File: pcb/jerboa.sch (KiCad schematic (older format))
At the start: 25 parts, among them P101 SWD_TC, U101 STM32L051K8U6

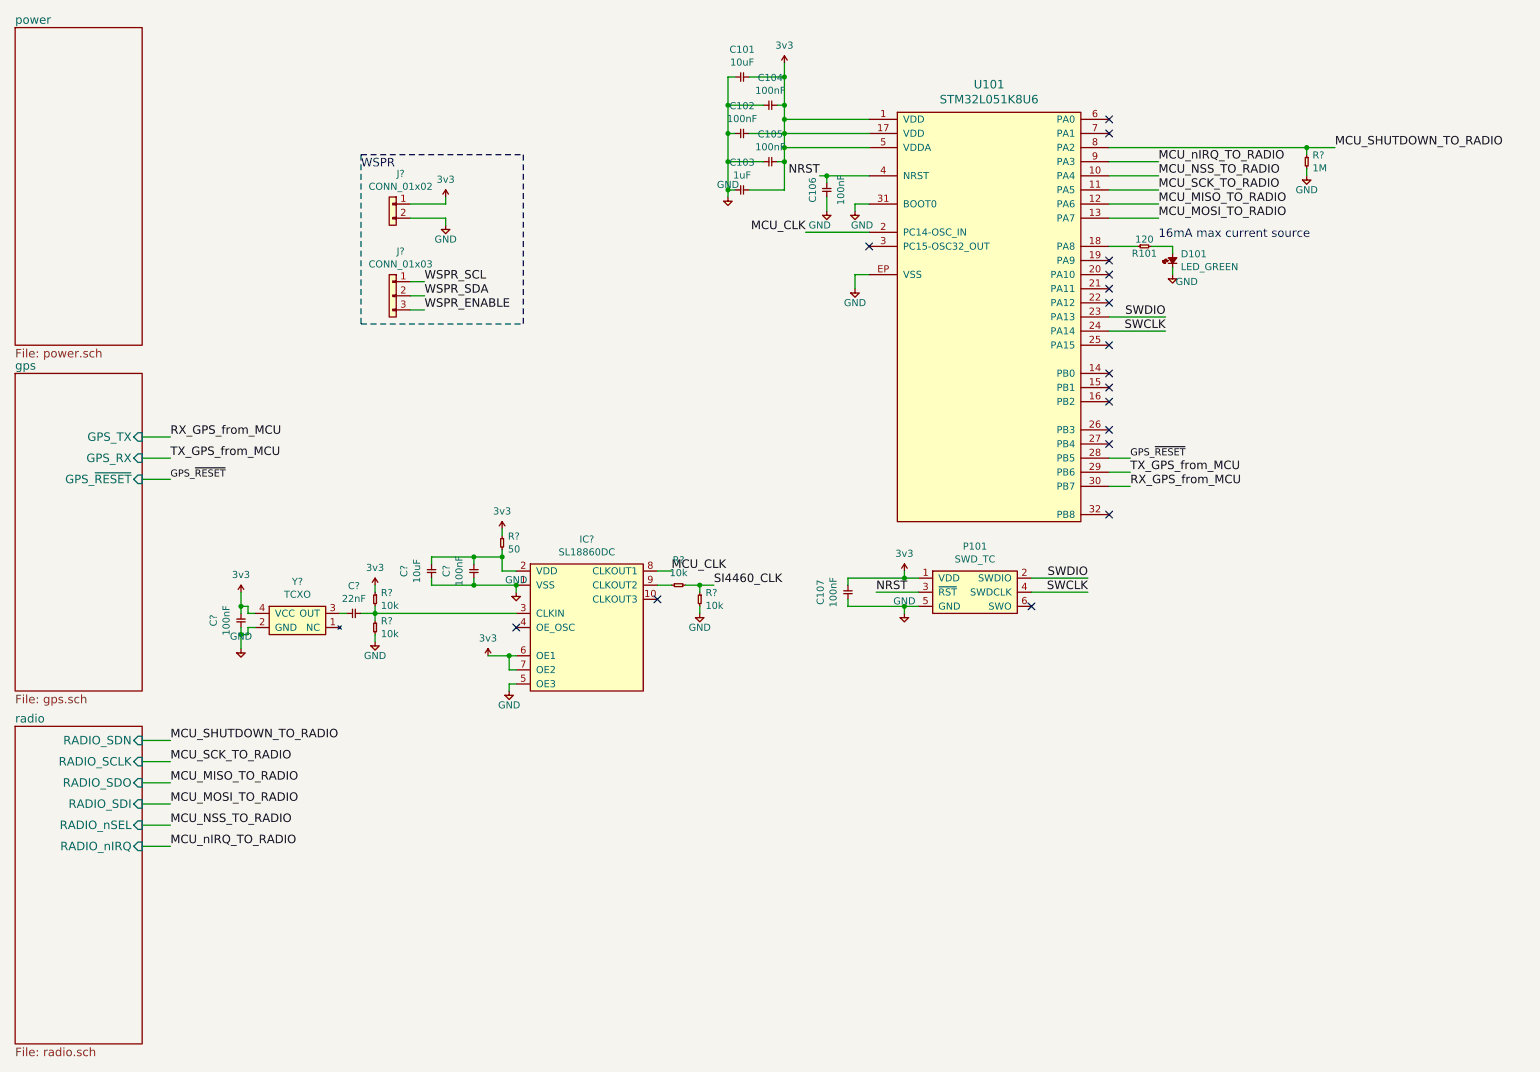
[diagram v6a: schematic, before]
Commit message: WIP: create and add componenents for the micrf rtty radio, also do some work on schematic
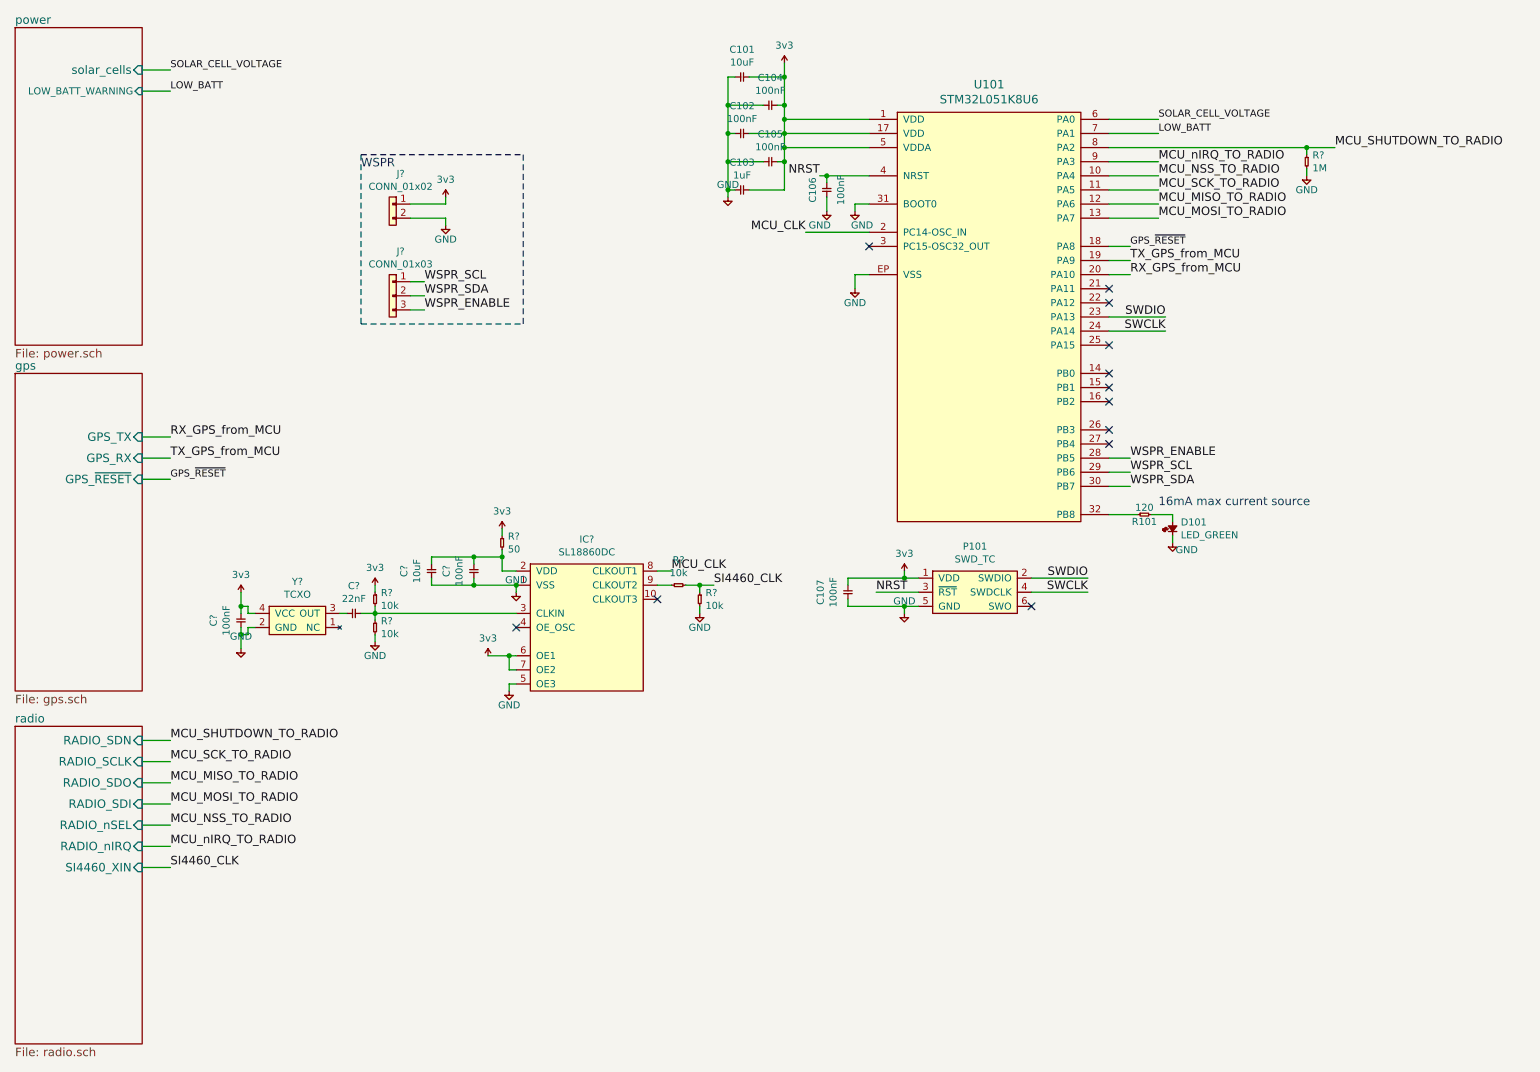
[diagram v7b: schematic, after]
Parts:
- J?: Farnell (none) -> 1593459
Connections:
- net GPS_~RESET: now also U101.18 (PA8); no longer U101.28 (PB5)
- net RX_GPS_from_MCU: now also U101.20 (PA10); no longer U101.30 (PB7)
- net TX_GPS_from_MCU: now also U101.19 (PA9); no longer U101.29 (PB6)
- net WSPR_ENABLE: now also U101.28 (PB5)
- net WSPR_SCL: now also U101.29 (PB6)
- net WSPR_SDA: now also U101.30 (PB7)
- net at R101.1: now also U101.32 (PB8); no longer U101.18 (PA8)
- net SOLAR_CELL_VOLTAGE: now reaches U101.6 (PA0)
- net LOW_BATT: now reaches U101.7 (PA1)
- no-connect marks 17 -> 12
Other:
- moved on the sheet: D101, R101
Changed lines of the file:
@@
 F0 "power" 60
 F1 "power.sch" 60
+F2 "solar_cells" I R 1400 800 60
+F3 "LOW_BATT_WARNING" I R 1400 950 50
 $EndSheet
 $Sheet
@@
 $EndSheet
 $Comp
-L STM32L051K8U6:STM32L051K8U6 U101
-U 1 1 5A37D9A9
-P 7400 2500
-F 0 "U101" H 7400 4097 60  0000 C CNN
-F 1 "STM32L051K8U6" H 7400 3991 60  0000 C CNN
-F 2 "agg:QFN-32-EP-ST" H 7050 800 60  0001 L CNN
-F 3 "http://www.st.com/resource/en/datasheet/stm32l051t8.pdf" H 7050 700 60  0001 L CNN
-F 4 "2488323" H 7050 600 60  0001 L CNN "Farnell"
-	1    7400 2500
-	1    0    0    -1
-$EndComp
-$Comp
 L agg-kicad:GND #PWR01
 U 1 1 5A3E3DF5
@@
 L agg-kicad:LED D101
 U 1 1 5A3E82EC
-P 8700 2200
-F 0 "D101" V 8796 2142 50  0000 R CNN
-F 1 "LED_GREEN" V 8705 2142 50  0000 R CNN
-F 2 "agg:0603-LED" H 8700 2200 50  0001 C CNN
-F 3 "http://www.farnell.com/datasheets/2057314.pdf?_ga=2.205110360.971487712.1514028244-506493331.1509210212&_gac=1.118829563.1511728794.Cj0KCQiA6enQBRDUARIsAGs1YQiJE2FAEjDkPfQxMJDRdXOREIvhi5-XX62hZWxB6j9IyKlXVrhl04oaArmMEALw_wcB" H 8700 2200 50  0001 C CNN
-F 4 "2575345" H 8700 2200 60  0001 C CNN "Farnell"
-	1    8700 2200
+P 8700 4100
+F 0 "D101" V 8796 4042 50  0000 R CNN
+F 1 "LED_GREEN" V 8705 4042 50  0000 R CNN
+F 2 "agg:0603-LED" H 8700 4100 50  0001 C CNN
+F 3 "http://www.farnell.com/datasheets/2057314.pdf?_ga=2.205110360.971487712.1514028244-506493331.1509210212&_gac=1.118829563.1511728794.Cj0KCQiA6enQBRDUARIsAGs1YQiJE2FAEjDkPfQxMJDRdXOREIvhi5-XX62hZWxB6j9IyKlXVrhl04oaArmMEALw_wcB" H 8700 4100 50  0001 C CNN
+F 4 "2575345" H 8700 4100 60  0001 C CNN "Farnell"
+	1    8700 4100
 	0    -1   -1   0
 $EndComp
@@
 L agg-kicad:R R101
 U 1 1 5A3E86C8
-P 8450 2050
-F 0 "R101" H 8500 2000 50  0000 C CNN
-F 1 "120" H 8500 2100 50  0000 C CNN
-F 2 "agg:0402" H 8450 2050 50  0001 C CNN
-F 3 "" H 8450 2050 50  0001 C CNN
-F 4 "9239120" H 8450 2050 60  0001 C CNN "Farnell"
-	1    8450 2050
+P 8450 3950
+F 0 "R101" H 8500 3900 50  0000 C CNN
+F 1 "120" H 8500 4000 50  0000 C CNN
+F 2 "agg:0402" H 8450 3950 50  0001 C CNN
+F 3 "" H 8450 3950 50  0001 C CNN
+F 4 "9239120" H 8450 3950 60  0001 C CNN "Farnell"
+	1    8450 3950
 	1    0    0    -1
 $EndComp
@@
 L agg-kicad:GND #PWR08
 U 1 1 5A3EA11D
-P 8700 2250
-F 0 "#PWR08" H 8570 2290 50  0001 L CNN
-F 1 "GND" H 8800 2200 50  0000 C CNN
-F 2 "" H 8700 2250 60  0001 C CNN
-F 3 "" H 8700 2250 60  0001 C CNN
-	1    8700 2250
-	1    0    0    -1
-$EndComp
-Text Notes 8600 2000 0    60   ~ 0
+P 8700 4150
+F 0 "#PWR08" H 8570 4190 50  0001 L CNN
+F 1 "GND" H 8800 4100 50  0000 C CNN
+F 2 "" H 8700 4150 60  0001 C CNN
+F 3 "" H 8700 4150 60  0001 C CNN
+	1    8700 4150
+	1    0    0    -1
+$EndComp
+Text Notes 8600 3900 0    60   ~ 0
 16mA max current source
 $Comp
@@
 Connection ~ 6250 1550
 Wire Wire Line
-	8250 2050 8450 2050
-Wire Wire Line
-	8700 2250 8700 2200
-Wire Wire Line
-	8700 2100 8700 2050
-Wire Wire Line
-	8700 2050 8550 2050
+	8250 3950 8450 3950
+Wire Wire Line
+	8700 4150 8700 4100
+Wire Wire Line
+	8700 4000 8700 3950
+Wire Wire Line
+	8700 3950 8550 3950
 Wire Wire Line
 	6450 1750 6550 1750
@@
 Wire Wire Line
 	6200 1550 6250 1550
-Text Label 8400 3650 0    60   ~ 0
+Text Label 8400 2150 0    60   ~ 0
 TX_GPS_from_MCU
-Text Label 8400 3750 0    60   ~ 0
+Text Label 8400 2250 0    60   ~ 0
 RX_GPS_from_MCU
-Wire Wire Line
-	8250 3750 8400 3750
 NoConn ~ 6550 2050
-NoConn ~ 8250 1150
-NoConn ~ 8250 1250
-NoConn ~ 8250 2150
-NoConn ~ 8250 2250
 NoConn ~ 8250 2350
 NoConn ~ 8250 2450
@@
 NoConn ~ 8250 3150
 NoConn ~ 8250 3350
-NoConn ~ 8250 3950
 Wire Wire Line
 	6400 4600 6800 4600
@@
 F6 "RADIO_nSEL" I R 1400 6150 60
 F7 "RADIO_nIRQ" I R 1400 6300 60
+F8 "SI4460_XIN" I R 1400 6450 60
 $EndSheet
 Wire Wire Line
@@
 Text Label 1600 6300 0    60   ~ 0
 MCU_nIRQ_TO_RADIO
-Wire Wire Line
-	8400 3650 8250 3650
 $Comp
 L agg-kicad:R R?
@@
 Text Label 1600 3700 0    50   ~ 0
 GPS_~RESET
-Text Label 8400 3550 0    50   ~ 0
+Text Label 8400 2050 0    50   ~ 0
 GPS_~RESET
 Wire Wire Line
-	8400 3550 8250 3550
+	8400 2050 8250 2050
 $Comp
 L agg-kicad:SL18860DC IC?
@@
 F 2 "" H 3200 2300 50  0001 C CNN
 F 3 "" H 3200 2300 50  0001 C CNN
+F 4 "1593459" H 3200 2300 50  0001 C CNN "Farnell"
 	1    3200 2300
 	1    0    0    -1
@@
 Wire Wire Line
 	2850 4650 2800 4650
+Text Label 8400 3650 0    60   ~ 0
+WSPR_SCL
+Text Label 8400 3750 0    60   ~ 0
+WSPR_SDA
+Text Label 8400 3550 0    60   ~ 0
+WSPR_ENABLE
+Wire Wire Line
+	8250 2150 8400 2150
+Wire Wire Line
+	8400 2250 8250 2250
+$Comp
+L STM32L051K8U6:STM32L051K8U6 U101
+U 1 1 5A37D9A9
+P 7400 2500
+F 0 "U101" H 7400 4097 60  0000 C CNN
+F 1 "STM32L051K8U6" H 7400 3991 60  0000 C CNN
+F 2 "agg:QFN-32-EP-ST" H 7050 800 60  0001 L CNN
+F 3 "http://www.st.com/resource/en/datasheet/stm32l051t8.pdf" H 7050 700 60  0001 L CNN
+F 4 "2488323" H 7050 600 60  0001 L CNN "Farnell"
+	1    7400 2500
+	1    0    0    -1
+$EndComp
+Wire Wire Line
+	8250 3550 8400 3550
+Wire Wire Line
+	8400 3650 8250 3650
+Wire Wire Line
+	8250 3750 8400 3750
+Wire Wire Line
+	1400 950  1600 950
+Wire Wire Line
+	1600 800  1400 800
+Text Label 8600 1150 0    50   ~ 0
+SOLAR_CELL_VOLTAGE
+Wire Wire Line
+	8600 1150 8250 1150
+Text Label 8600 1250 0    50   ~ 0
+LOW_BATT
+Wire Wire Line
+	8250 1250 8600 1250
+Text Label 1600 800  0    50   ~ 0
+SOLAR_CELL_VOLTAGE
+Text Label 1600 950  0    50   ~ 0
+LOW_BATT
+Text Label 1600 6450 0    60   ~ 0
+SI4460_CLK
+Wire Wire Line
+	1600 6450 1400 6450
 $EndSCHEMATC

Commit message: Finish schematic, generate first BOM
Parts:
- added R7, R8: 4k7, agg:0402, symbol agg-kicad:R
- C1, C4: renamed from C?; Farnell 1288282 -> 2533923
- C10: renamed from C106; Farnell 1288282 -> 2533923
- C11: renamed from C107; Farnell 1288282 -> 2533923
- C2: renamed from C?; Farnell 1288282 -> 1828865
- C3: renamed from C?; Farnell 1288282 -> 2611904
- C5: renamed from C101; footprint (none) -> agg:0402; Farnell Value -> 2611904
- C6: renamed from C102; Farnell 1288282 -> 2533923
- C7: renamed from C103; Farnell 1327658 -> 1758879
- C8: renamed from C104; Farnell 1288282 -> 2533923
- C9: renamed from C105; Farnell 1288282 -> 2533923
- IC1: renamed from IC?; Digikey (none) -> SL18860DC-ND
- J2: renamed from J?; footprint (none) -> agg:SIL-254P-03
- R1, R2, R4, R5: renamed from R?; footprint (none) -> agg:0402; Farnell Value -> 2331444
- R3: renamed from R?; footprint (none) -> agg:0603; Farnell Value -> 2112878
- gave numbers to parts that had none: 3
- renumbered D101 to D1, P101 to P1, R101 to R6, U101 to U1
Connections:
- net labels added: DAC_NCS, I2C_SCL, I2C_SDA, MCU_MISO, MCU_MOSI, MCU_SCK, MICRF_EN, SI4460_NSS, TMP_ALERT
- net labels removed: MCU_MISO_TO_RADIO, MCU_MOSI_TO_RADIO, MCU_NSS_TO_RADIO, MCU_SCK_TO_RADIO, WSPR_SCL, WSPR_SDA
- wire segments 129 -> 148
- no-connect marks 12 -> 9
